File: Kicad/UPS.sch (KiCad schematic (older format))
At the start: 53 parts, among them J1 USB_B_Micro, J10 GET_UP_SERVO_RIGHT, J11 SPI, J12 I2C, J2 Conn_02x20_Odd_Even, J3 X_HEAD_PAN, J4 Y_HEAD_PAN, J5 X_CLAW, J6 Y_CLAW, J7 MOTOR_LEFT, J8 MOTOR_RIGHT, J9 GET_UP_SERVO_LEFT, Q1 Q_PNP_BCE, SW1 SW_Push, U1 ip5306, U2 CW2015, U3 ETA1096

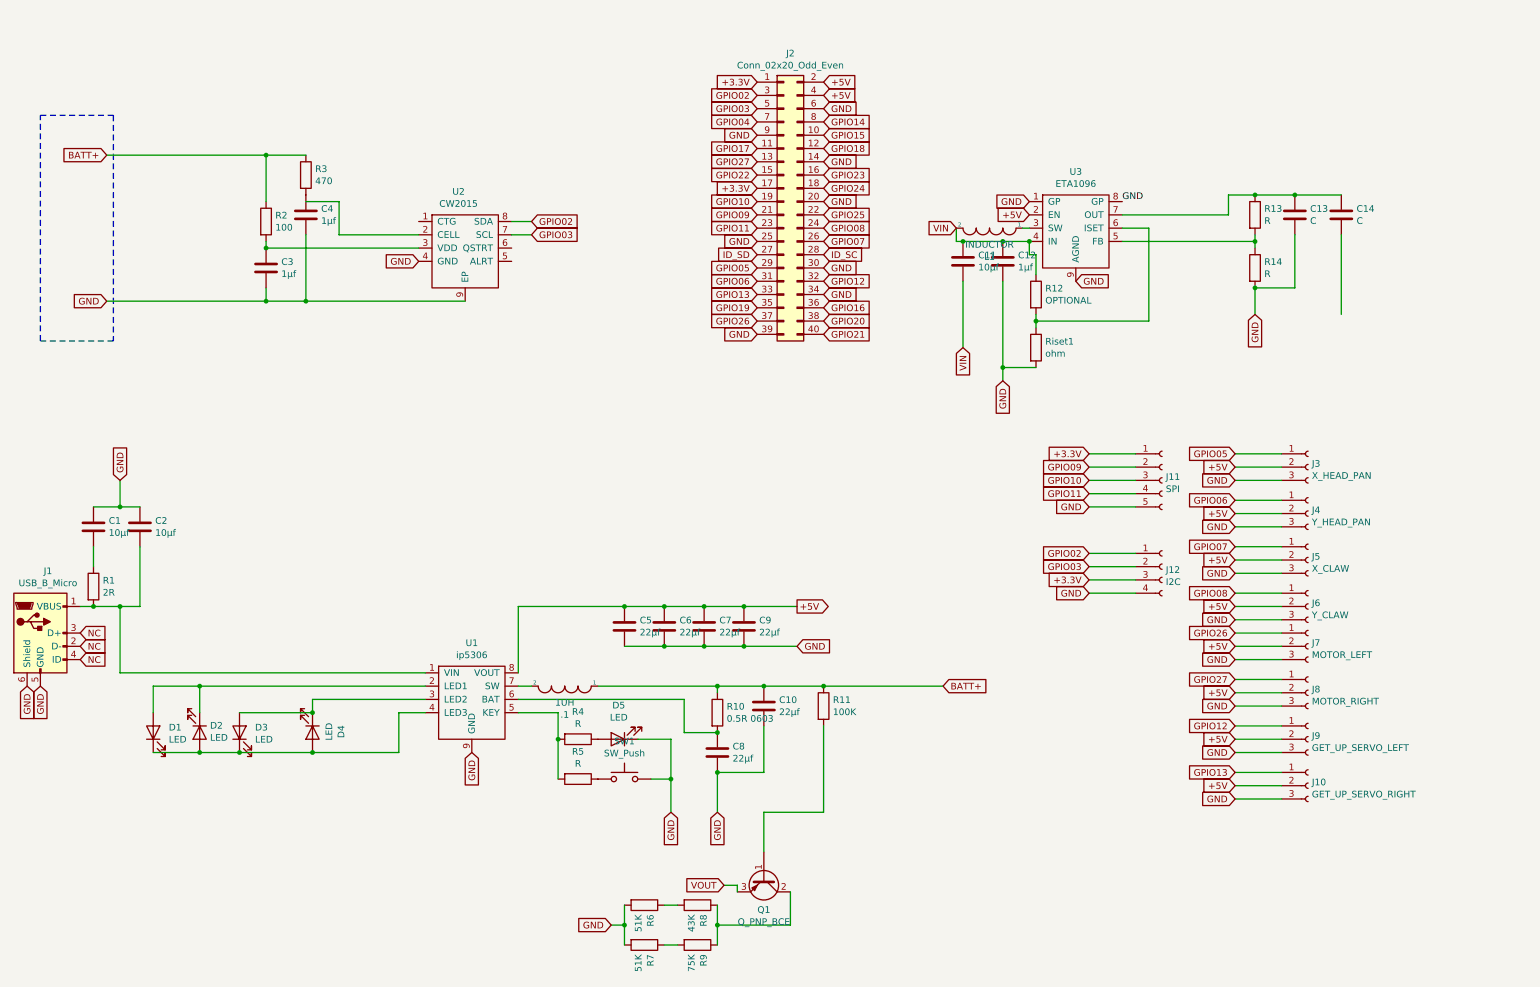
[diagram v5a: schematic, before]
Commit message: Add Datasheet of IP5306
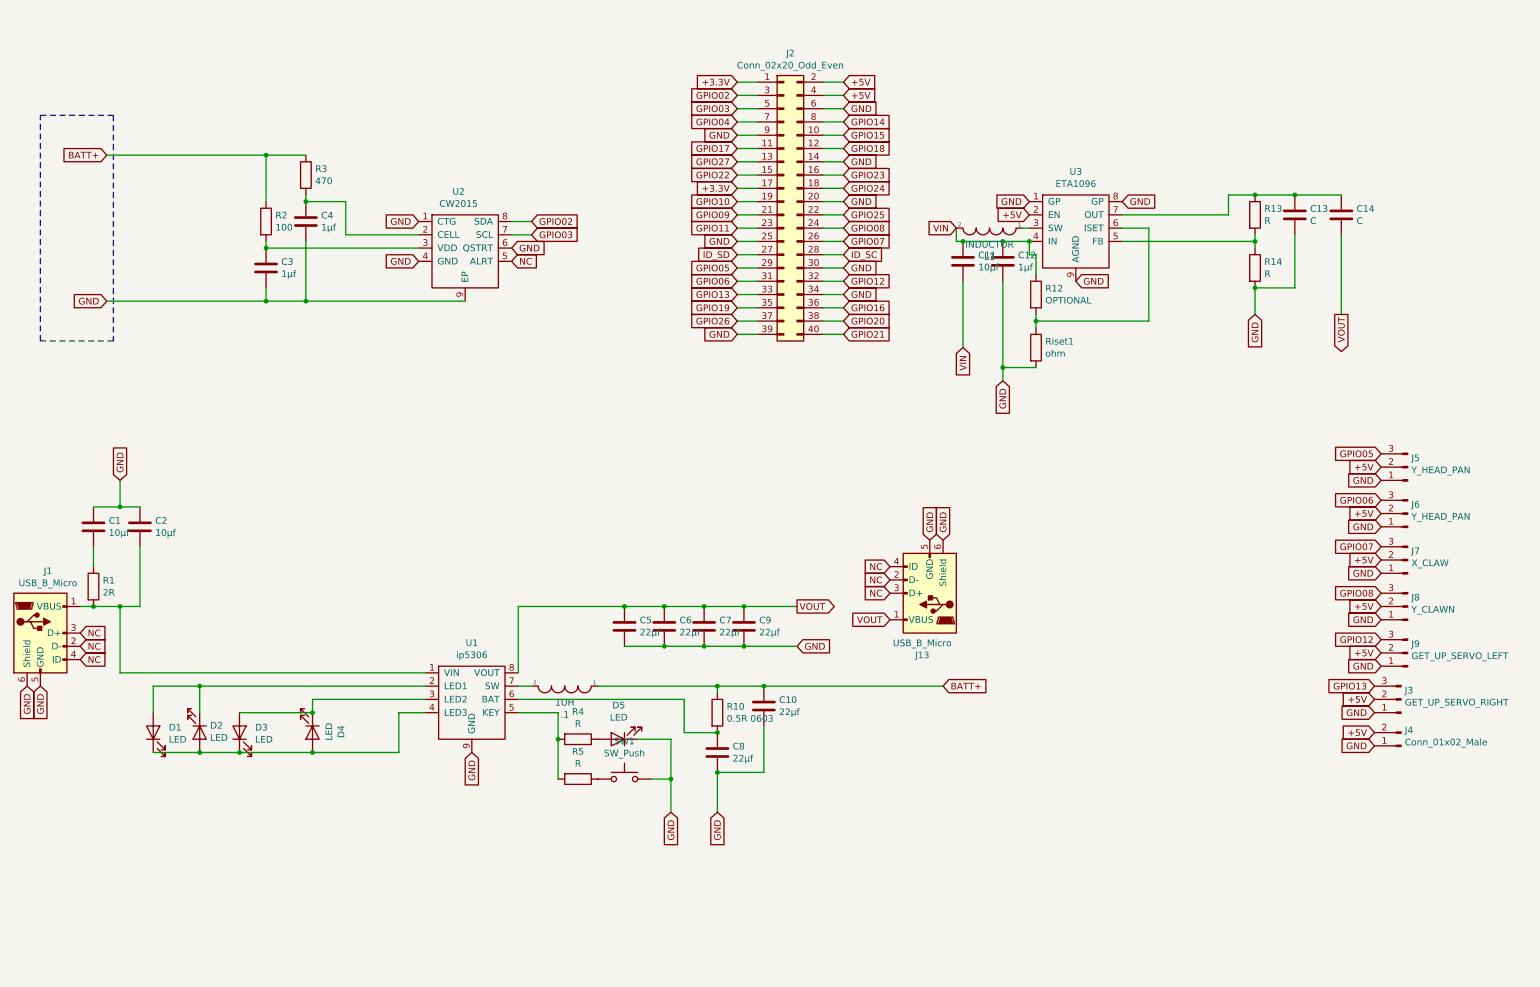
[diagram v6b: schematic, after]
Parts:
- removed J10: GET_UP_SERVO_RIGHT, symbol Connector:Conn_01x03_Female
- removed J11: SPI, symbol Connector:Conn_01x05_Female
- removed J12: I2C, symbol Connector:Conn_01x04_Female
- removed J3: X_HEAD_PAN, symbol Connector:Conn_01x03_Female
- removed J4: Y_HEAD_PAN, symbol Connector:Conn_01x03_Female
- removed J5: X_CLAW, symbol Connector:Conn_01x03_Female
- removed J6: Y_CLAW, symbol Connector:Conn_01x03_Female
- removed J7: MOTOR_LEFT, symbol Connector:Conn_01x03_Female
- removed J8: MOTOR_RIGHT, symbol Connector:Conn_01x03_Female
- removed J9: GET_UP_SERVO_LEFT, symbol Connector:Conn_01x03_Female
- removed Q1: Q_PNP_BCE, symbol Device:Q_PNP_BCE
- removed R11: 100K, symbol Device:R
- removed R6, R7: 51K, symbol Device:R
- removed R8: 43K, symbol Device:R
- removed R9: 75K, symbol Device:R
- added J13: USB_B_Micro, symbol Connector:USB_B_Micro
- added J3: GET_UP_SERVO_RIGHT, Connector_PinSocket_2.54mm:PinSocket_1x03_P2.54mm_Horizontal, symbol Connector:Conn_01x03_Male
- added J4: Conn_01x02_Male, Connector_PinSocket_2.54mm:PinSocket_1x02_P2.54mm_Horizontal, symbol Connector:Conn_01x02_Male
- added J5, J6: Y_HEAD_PAN, Connector_PinSocket_2.54mm:PinSocket_1x03_P2.54mm_Horizontal, symbol Connector:Conn_01x03_Male
- added J7: X_CLAW, Connector_PinSocket_2.54mm:PinSocket_1x03_P2.54mm_Horizontal, symbol Connector:Conn_01x03_Male
- added J8: Y_CLAWN, Connector_PinSocket_2.54mm:PinSocket_1x03_P2.54mm_Horizontal, symbol Connector:Conn_01x03_Male
- added J9: GET_UP_SERVO_LEFT, symbol Connector:Conn_01x03_Male
- D1, D2, D3, D4, D5: footprint (none) -> LED_SMD:LED_01005_0402Metric
- J2: footprint (none) -> Connector_PinSocket_2.54mm:PinSocket_2x20_P2.54mm_Vertical
- SW1: footprint (none) -> Button_Switch_SMD:SW_SPST_CK_RS282G05A3
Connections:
- net +5V: now also J3.2 (Pin_2), J4.2 (Pin_2), J5.2 (Pin_2), J6.2 (Pin_2), J7.2 (Pin_2), J8.2 (Pin_2), J9.2 (Pin_2); no longer C5.1, C6.1, C7.1, C9.1, U1.8 (VOUT)
- net GND: now also U2.1 (CTG), U2.6 (QSTRT), J13.5 (GND), J13.6 (Shield), J3.1 (Pin_1), J4.1 (Pin_1), J5.1 (Pin_1), J6.1 (Pin_1), J7.1 (Pin_1), J8.1 (Pin_1), J9.1 (Pin_1)
- net GPIO05: now also J5.3 (Pin_3)
- net GPIO06: now also J6.3 (Pin_3)
- net GPIO07: now also J7.3 (Pin_3)
- net GPIO08: now also J8.3 (Pin_3)
- net GPIO12: now also J9.3 (Pin_3)
- net GPIO13: now also J3.3 (Pin_3)
- net NC: now also U2.5 (ALRT), J13.2 (D-), J13.3 (D+), J13.4 (ID)
- net VOUT: now also C14.2, C5.1, C6.1, C7.1, C9.1, U1.8 (VOUT), J13.1 (VBUS)
- net at U2.2 (CELL): now also C4.1, R3.2
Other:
- moved on the sheet: C4
